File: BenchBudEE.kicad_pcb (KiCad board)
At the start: 4 copper layers, 165.1 x 63.5 mm, 49 parts, among them K1 1461069-5, P2 CONN_2, P3 CONN_3X2, Q1 1461069-5, U1 6N137S-TA1, U10 MCP3901, U11 LMT84, U2 AP5726, U4 OPA4170, U9 LM324

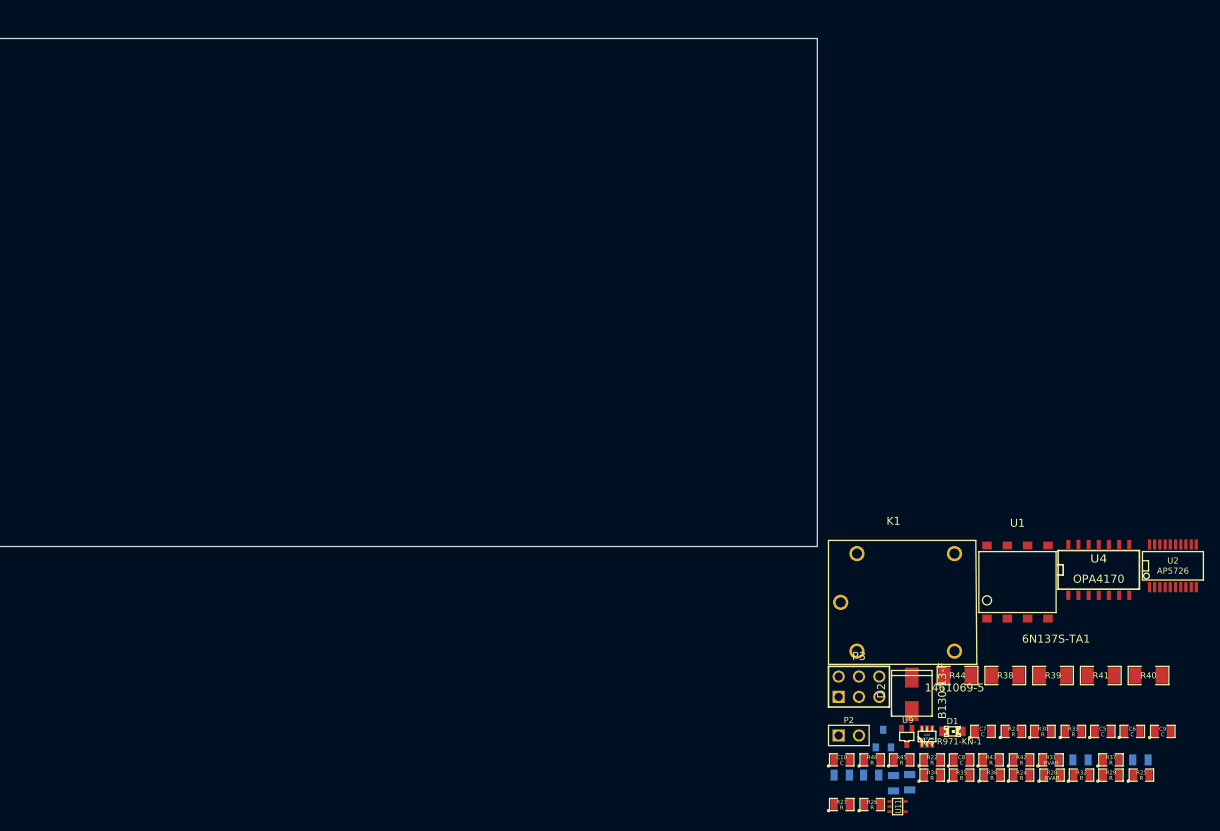
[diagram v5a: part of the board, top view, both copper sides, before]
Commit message: 5.4 Video 2/2 Associating and Placing the Thermocouple Module
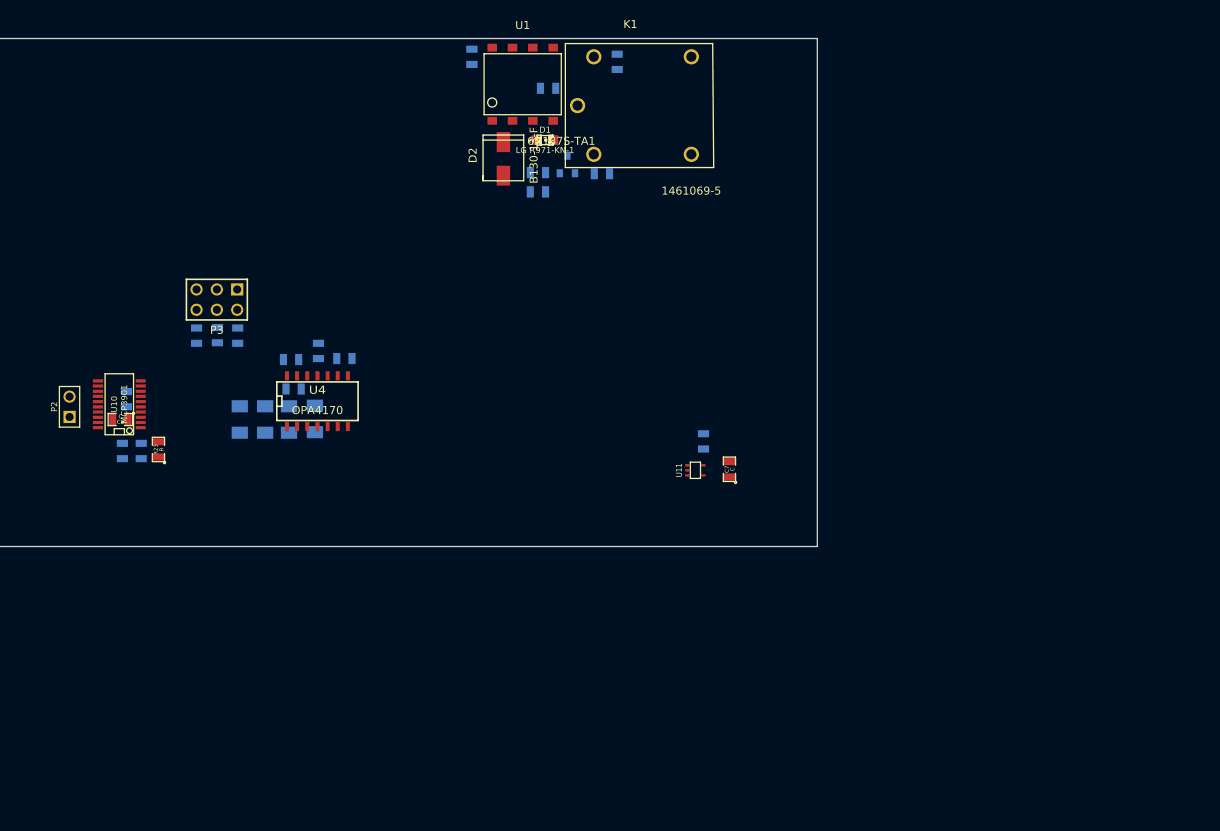
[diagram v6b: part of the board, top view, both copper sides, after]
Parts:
- removed R22, R24, R25, R26, R27, R29, R30, R32, R33, R34, R35, R36, R37: R, SM0805
- removed R28, R31: RVAR, SM0805
- removed U2: AP5726, SSOP20
- removed U9: LM324, SOT323
- added R47: 0, SM0805, B.Cu at (213.1, 142.0)
- added R48: 0, SM0805, B.Cu at (285.2, 147.3)
- C10, C5, C6, C9, R38, R39, R40, R41, R42, R43, R45, R46: moved to B.Cu
- R44: footprint SM1206 -> SM0805; moved to B.Cu
- U10: footprint sot323-6 -> SSOP20
- moved C6 131.0 mm to (212.6, 148.5), turned to 270 degrees
- moved C5 125.2 mm to (214.9, 148.5), turned to 270 degrees
- moved C9 115.8 mm to (237.1, 136.0), turned to 90 degrees
- moved C8 113.4 mm to (212.3, 144.5), turned to 180 degrees
- moved R23 112.5 mm to (217.1, 148.3), turned to 90 degrees
- moved U10 109.2 mm to (212.2, 142.6), turned to 90 degrees
- moved R40 109.0 mm to (236.7, 144.5), turned to 90 degrees
- moved R39 106.6 mm to (227.3, 144.5), turned to 270 degrees
- moved R41 106.4 mm to (233.4, 144.5), turned to 90 degrees
- moved P2 105.7 mm to (206.0, 142.9), turned to 90 degrees
- moved R1 105.0 mm to (256.3, 99.2)
- moved R44 104.2 mm to (221.9, 134.0), turned to 90 degrees
- moved R43 100.8 mm to (233.7, 137.0), turned to 180 degrees
- moved R45 100.7 mm to (224.5, 134.0), turned to 90 degrees
- moved U4 99.9 mm to (237.0, 142.1)
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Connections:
- C7 pad 2: N-0000086 (its old number) -> AGND
- C8 pad 1: N-0000062 -> /Thermocouple/CHO+
- C8 pad 2: N-0000085 (its old number) -> /Thermocouple/CH0-
- K1 pad 1: (no net) -> /Relay/REALY_COM
- K1 pad 3: (no net) -> /Relay/RELAY_NO
- K1 pad 4: (no net) -> /Relay/RELAY_NC
- P2 pad 1: N-0000066 -> N-0000063
- P2 pad 2: N-0000067 (its old number) -> N-0000074
- P3 pad 1: N-0000083 (its old number) -> N-0000066
- P3 pad 3: N-0000083 (its old number) -> N-0000066
- P3 pad 5: N-0000083 (its old number) -> N-0000066
- R38 pad 1: N-0000085 (its old number) -> AGND
- R38 pad 2: N-0000075 -> N-0000073
- R39 pad 1: N-0000062 -> /Thermocouple/CHO+
- R39 pad 2: N-0000074 -> N-0000072
- R40 pad 1: N-0000074 -> N-0000072
- R40 pad 2: (no net) -> N-0000071
- R41 pad 1: N-0000075 -> N-0000073
- R42 pad 1: N-0000063 -> N-0000071
- R42 pad 2: (no net) -> N-0000066
- R43 pad 1: (no net) -> N-0000080
- R44 pad 1: N-0000087 (its old number) -> N-0000080
- R45 pad 1: N-0000087 (its old number) -> N-0000080
- R46 pad 1: N-0000087 (its old number) -> N-0000080
- U10 pad 4: N-0000062 -> /Thermocouple/CHO+
- U10 pad 5: N-0000085 (its old number) -> /Thermocouple/CH0-
- U10 pad 6: N-0000086 (its old number) -> /Thermocouple/CH1-
- U11 pad 1: N-0000086 (its old number) -> AGND
- U11 pad 2: N-0000086 (its old number) -> AGND
- U11 pad 3: N-0000071 -> /Thermocouple/CH1+
- U11 pad 5: N-0000086 (its old number) -> AGND
- U4 pad 1: N-00000124 -> /Thermocouple/CHO+
- U4 pad 10: (no net) -> /Thermocouple/TC IN +
- U4 pad 12: (no net) -> /Thermocouple/TC IN -
- U4 pad 13: N-0000087 (its old number) -> N-0000080
- U4 pad 2: /Arduino/CURR_MEAS -> N-0000072
- U4 pad 3: N-00000126 -> N-0000073
- U4 pad 5: N-0000075 -> N-00000121
- U4 pad 6: N-0000074 -> /Arduino/CURR_MEAS
- U4 pad 7: N-0000062 -> N-00000119
- U4 pad 8: N-0000063 -> N-0000071
- U4 pad 9: N-0000083 (its old number) -> N-0000066

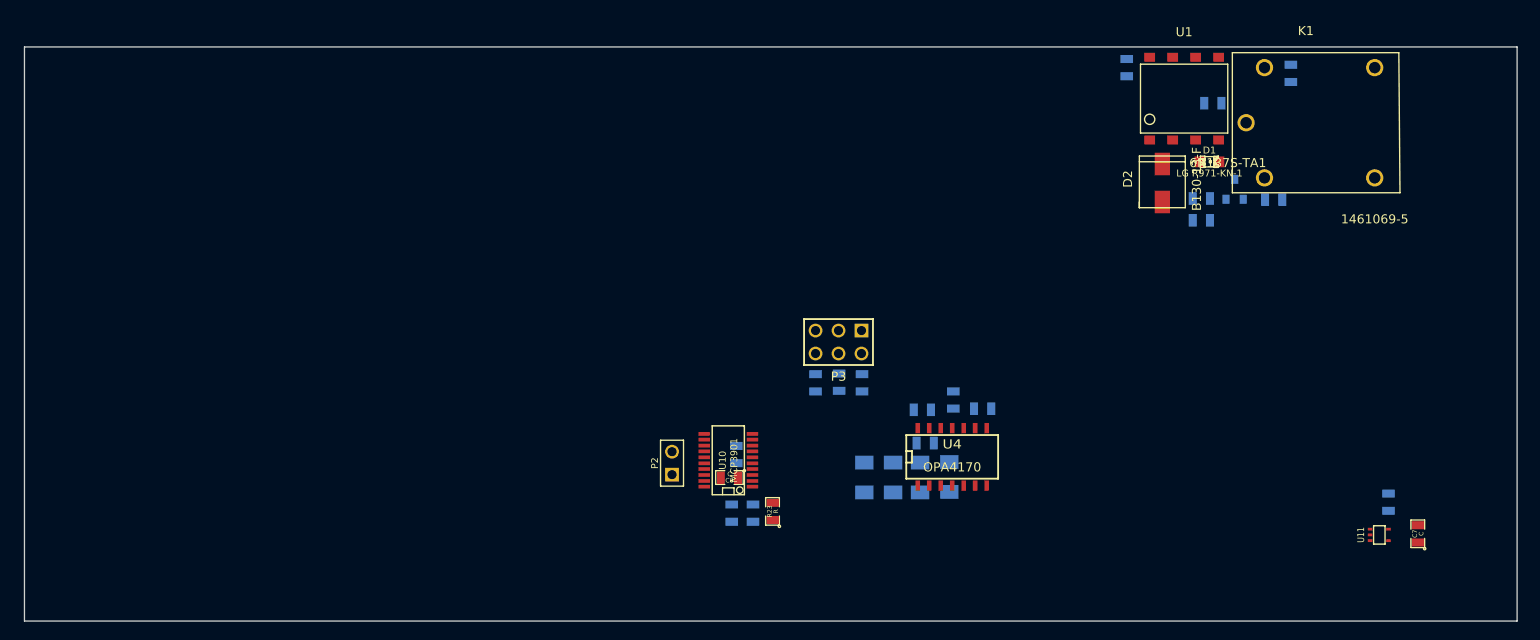
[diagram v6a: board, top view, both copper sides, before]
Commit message: 5.6 Video 2/2 Associating and Placing the Terminal/ATX Blocks
Created the 12pin, 3 pin and atx connector footprints and placed
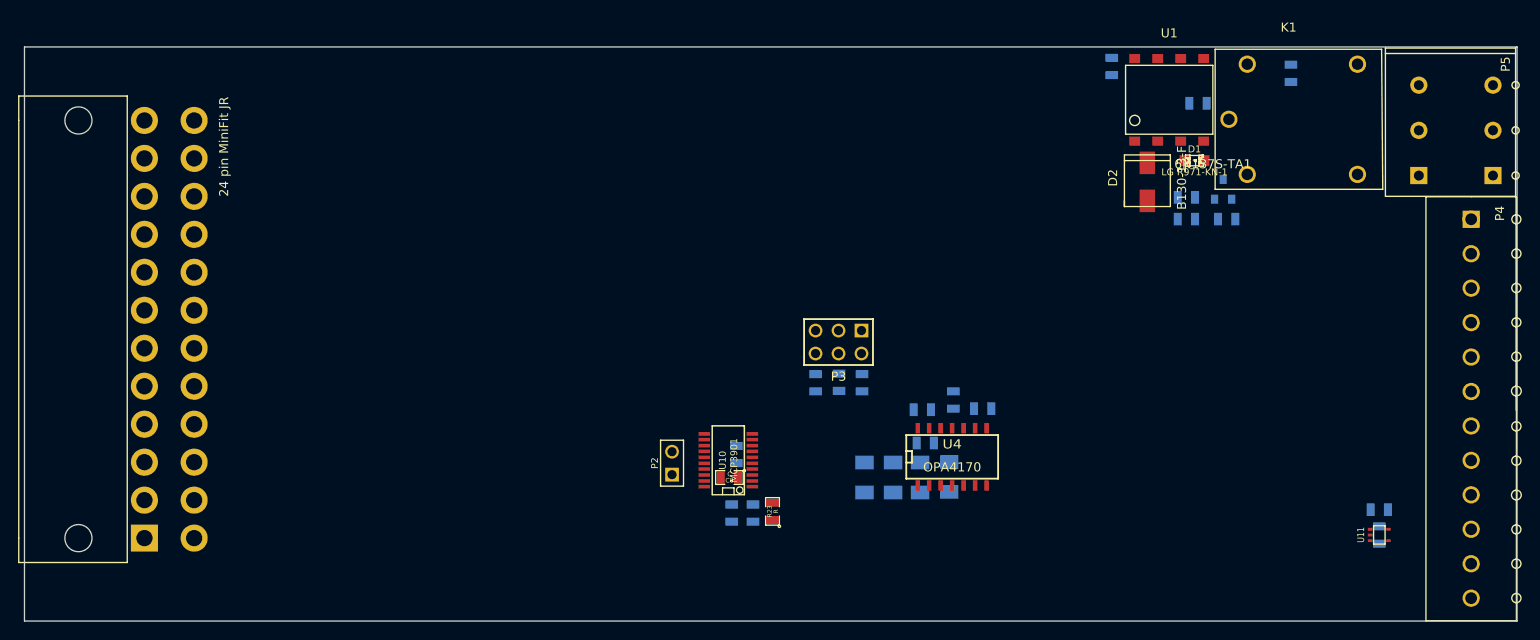
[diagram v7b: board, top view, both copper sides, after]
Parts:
- added P1: 24 pin MiniFit JR, ATX_Header, F.Cu at (140.3, 105.0)
- added P4: 12 Pin Terminal Block, 12pinPhoenixConnector, F.Cu at (294.4, 157.9)
- added P5: 3 Pin TB, 3pinPhoenixTerminalBlock, F.Cu at (296.8, 111.1)
- C7: moved to B.Cu
- moved R3 5.64 mm to (267.3, 116.0)
- moved C7 4.26 mm to (284.2, 150.9)
- moved K1 1.94 mm to (269.6, 111.0)
- moved D2 1.66 mm to (258.6, 113.9)
- moved R2 1.66 mm to (262.9, 113.5)
- moved R5 1.66 mm to (262.9, 116.0)
- moved D1 1.66 mm to (263.8, 109.5)
- moved R1 1.66 mm to (254.6, 99.1)
- moved U1 1.66 mm to (257.2, 107.3)
- moved R4 1.65 mm to (264.2, 103.1)
- moved R48 1.31 mm to (284.2, 148.1), turned to 0 degrees
- moved Q1 1.27 mm to (267.0, 112.6)
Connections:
- U10 pad 10: REF- -> (no net)
- U10 pad 15: N-0000062 -> (no net)
- U10 pad 16: N-0000061 -> (no net)
- U10 pad 9: REF+ -> (no net)

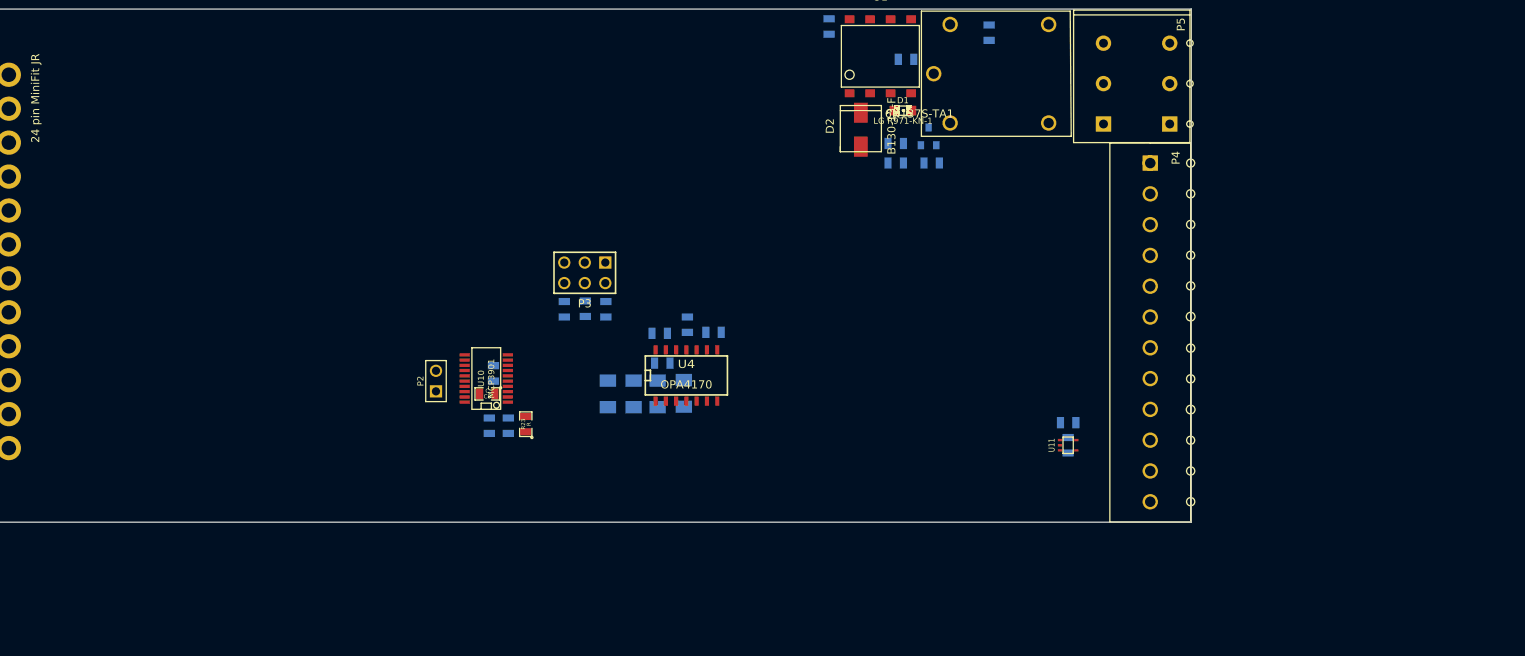
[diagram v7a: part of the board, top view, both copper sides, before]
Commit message: 5.6 Associating and Placing the Arduino Module
Added Arduino and 0805_blob footprints, placed arduino board
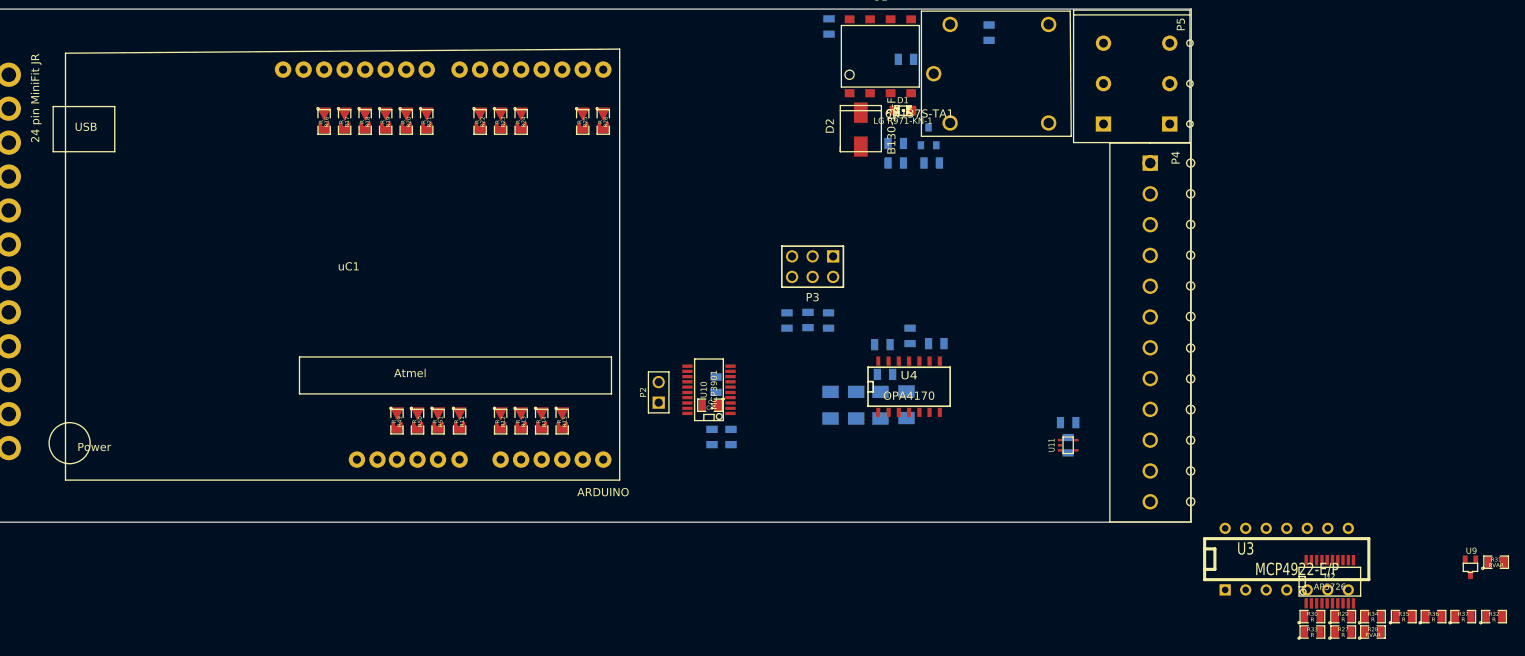
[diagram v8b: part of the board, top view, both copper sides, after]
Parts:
- added R11: R, SM0805_blob, F.Cu at (208.9, 148.0)
- added R12: R, SM0805_blob, F.Cu at (214.0, 148.0)
- added R13: R, SM0805_blob, F.Cu at (216.5, 148.0)
- added R14: R, SM0805_blob, F.Cu at (219.1, 148.0)
- added R15: R, SM0805_blob, F.Cu at (221.6, 148.0)
- added R16: R, SM0805_blob, F.Cu at (192.2, 110.9)
- added R17: R, SM0805_blob, F.Cu at (194.7, 110.9)
- added R18: R, SM0805_blob, F.Cu at (197.2, 110.9)
- added R19: R, SM0805_blob, F.Cu at (199.8, 110.9)
- added R20: R, SM0805_blob, F.Cu at (202.3, 110.9)
- added R21: R, SM0805_blob, F.Cu at (204.9, 110.9)
- added R22: R, SM0805_blob, F.Cu at (211.5, 110.9)
- added R24: R, SM0805_blob, F.Cu at (216.5, 110.9)
- added R25: R, SM0805_blob, F.Cu at (224.2, 110.9)
- added R26: R, SM0805_blob, F.Cu at (226.7, 110.9)
- added R27: R, SM0805, F.Cu at (318.3, 174.0)
- added R28: RVAR, SM0805, F.Cu at (321.9, 174.0)
- added R29: R, SM0805, F.Cu at (318.3, 172.1)
- added R30: R, SM0805, F.Cu at (314.5, 172.1)
- added R31: RVAR, SM0805, F.Cu at (337.2, 165.4)
- added R32: R, SM0805, F.Cu at (336.9, 172.1)
- added R33: R, SM0805, F.Cu at (314.5, 174.0)
- added R34: R, SM0805, F.Cu at (321.9, 172.1)
- added R35: R, SM0805, F.Cu at (325.8, 172.1)
- added R36: R, SM0805, F.Cu at (329.4, 172.1)
- added R37: R, SM0805, F.Cu at (333.1, 172.1)
- added R49: R, SM0805_blob, F.Cu at (201.2, 148.0)
- added R50: R, SM0805_blob, F.Cu at (203.7, 148.0)
- added R51: R, SM0805_blob, F.Cu at (206.2, 148.0)
- added U2: AP5726, SSOP20, F.Cu at (316.6, 167.8)
- added U3: MCP4922-E/P, DIP-14__300, F.Cu at (311.3, 165.0)
- added U9: LM324, SOT323, F.Cu at (334.0, 166.0)
- added uC1: ARDUINO, Arduino, F.Cu at (195.2, 129.8)
- R23: footprint SM0805 -> SM0805_blob
- moved R23 37.5 mm to (214.0, 110.9), turned to 270 degrees
- moved P3 28.2 mm to (252.6, 128.8)
- moved C10 27.6 mm to (261.6, 142.1)
- moved R41 27.6 mm to (261.0, 145.9)
- moved C5 27.6 mm to (242.5, 149.9)
- moved C6 27.6 mm to (240.2, 149.9)
- moved C8 27.6 mm to (239.9, 145.9)
- moved C9 27.6 mm to (264.7, 137.4)
- moved P2 27.6 mm to (233.6, 144.3)
- moved R38 27.6 mm to (258.0, 145.9)
- moved R39 27.6 mm to (254.8, 145.9)
- moved R40 27.6 mm to (264.2, 145.9)
- moved R42 27.6 mm to (267.9, 138.3)
- moved R44 27.6 mm to (249.4, 135.4)
- moved R45 27.6 mm to (252.0, 135.4)
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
